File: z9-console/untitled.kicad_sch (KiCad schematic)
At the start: 29 parts, among them U301 TLV76733DRVx, U302 B0505XT-1WR3, U303 LMR14006YDDCR

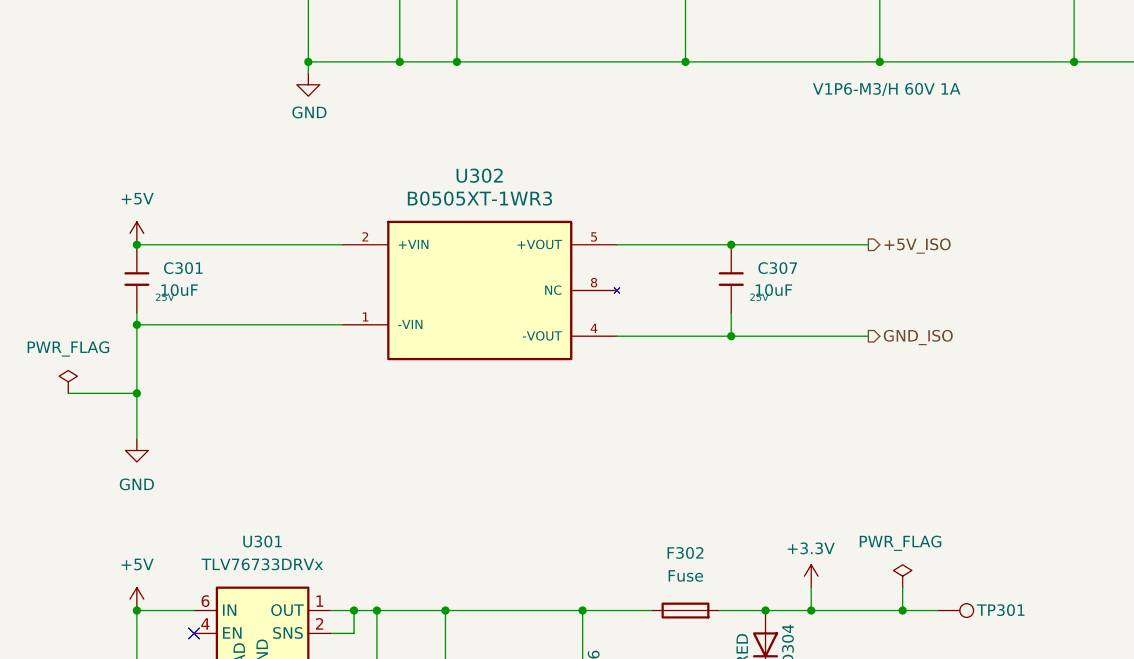
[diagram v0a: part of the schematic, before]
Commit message: Update schematic and project configuration
- Changed the starting number for annotation in the project configuration from 300 to 700.
- Removed the "+5V_ISO" label from the schematic.
- Adjusted the position of the "PE13" label.
- Added a new "VBATT" label in the schematic.
- Updated the "shared buzzer" sheet reference, changing its UUID and properties.
- Modified the pin configuration for the "BUZZER" input in the schematic.
- Cleaned up unused labels and adjusted pin placements for clarity.
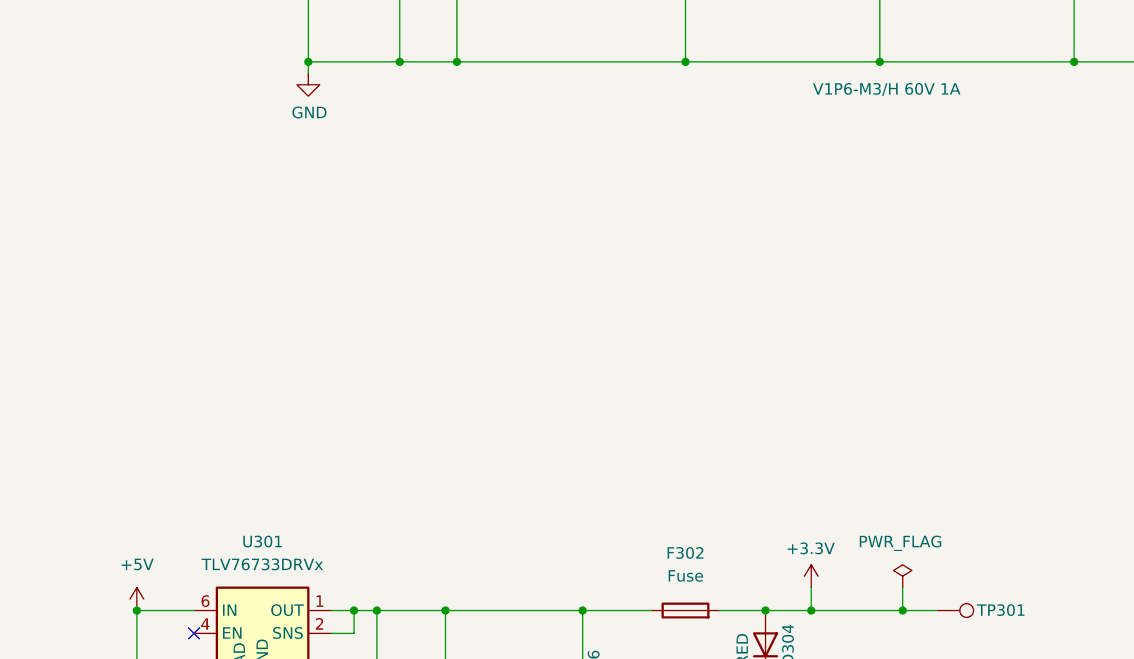
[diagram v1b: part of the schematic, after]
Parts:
- removed C301, C307: 10uF, dnt:C_0603_1608Metric, symbol dnt_global:0603,10uF,_25V
- removed U302: B0505XT-1WR3, dnt:B0505_Isolated_SMD, symbol dnt_global:B0505_Isolated_SMD

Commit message: Update KiCad project files and schematic references
- Changed active layer in z9-console.kicad_prl from 5 to 0.
- Removed a missing courtyard warning from z9-console.kicad_pro.
- Updated library footprint mismatch handling from ignore to error in z9-console.kicad_pro.
- Changed net conflict handling from warning to error in z9-console.kicad_pro.
- Updated silk over copper and silk overlap handling from warning to ignore in z9-console.kicad_pro.
- Changed via dangling handling from warning to error in z9-console.kicad_pro.
- Updated reference properties in shared_isolated_can.kicad_sch, changing several references from #PWR0954 and #PWR0955 to #PWR0105 and #PWR0106 respectively, and added project paths for new references.
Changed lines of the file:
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@@
 	(text "series 300"
 		(exclude_from_sim no)
-		(at 131.826 34.544 0)
+		(at 276.098 162.814 0)
 		(effects
 			(font
